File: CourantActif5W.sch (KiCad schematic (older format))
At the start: 2 parts, among them U23 ADC124S021CIMM_NOPB

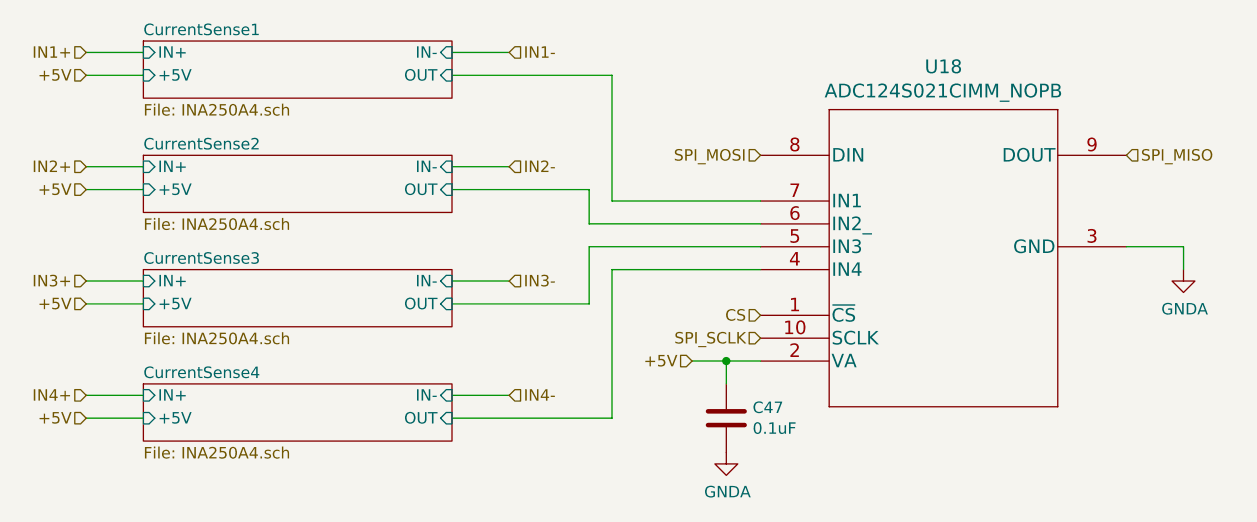
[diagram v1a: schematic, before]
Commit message: Changement pin pour switchs cannaux passifs
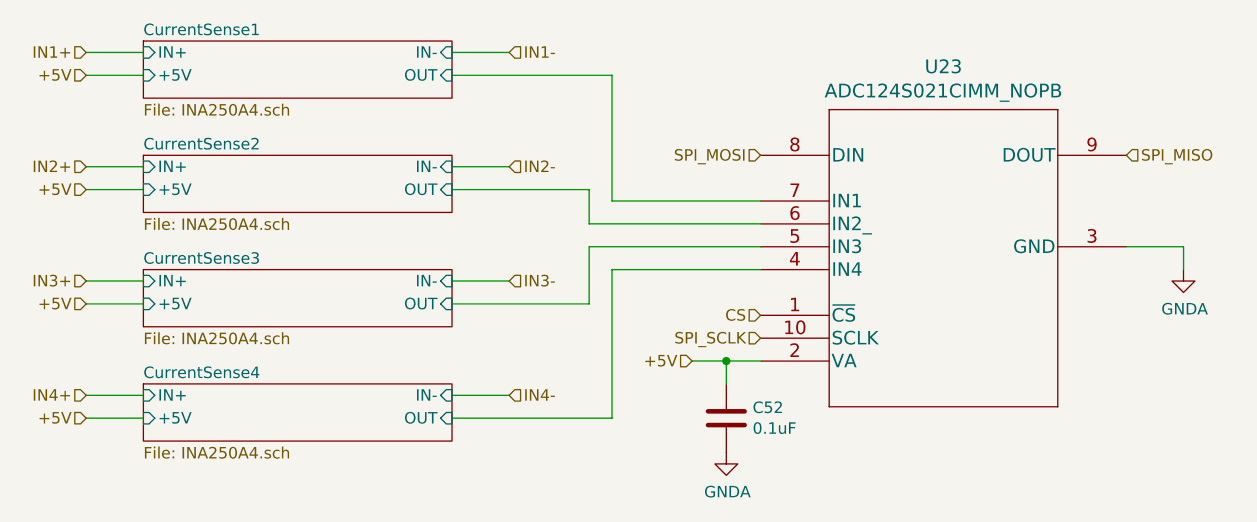
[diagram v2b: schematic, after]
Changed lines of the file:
@@
 $Descr A4 11693 8268
 encoding utf-8
-Sheet 24 80
+Sheet 29 80
 Title ""
 Date "2020-05-19"
@@
 AR Path="/5EEAF65F/5EDDD78D" Ref="U13"  Part="1"
 AR Path="/5EEC30AA/5EDDD78D" Ref="U18"  Part="1"
-F 0 "U18" H 6950 3537 60  0000 C CNN
+F 0 "U23" H 6950 3537 60  0000 C CNN
 F 1 "ADC124S021CIMM_NOPB" H 6950 3431 60  0000 C CNN
 F 2 "Package_SO:VSSOP-10_3x3mm_P0.5mm" H 6950 3390 60  0001 C CNN
@@
 AR Path="/5EEAF65F/5EDF45FB" Ref="C42"  Part="1"
 AR Path="/5EEC30AA/5EDF45FB" Ref="C47"  Part="1"
-F 0 "C47" H 6115 4346 50  0000 L CNN
+F 0 "C52" H 6115 4346 50  0000 L CNN
 F 1 "0.1uF" H 6115 4255 50  0000 L CNN
 F 2 "Capacitor_SMD:C_0402_1005Metric" H 6038 4150 50  0001 C CNN

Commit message: Routed most of the power
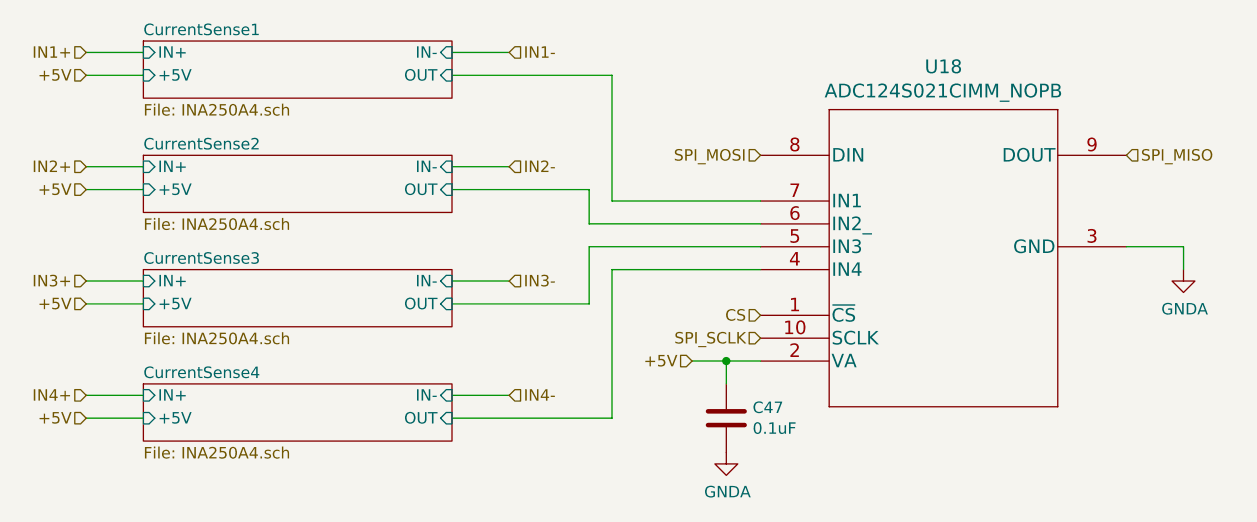
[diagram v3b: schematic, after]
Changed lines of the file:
@@
 $Descr A4 11693 8268
 encoding utf-8
-Sheet 29 80
+Sheet 24 80
 Title ""
 Date "2020-05-19"
@@
 AR Path="/5EEAF65F/5EDDD78D" Ref="U13"  Part="1"
 AR Path="/5EEC30AA/5EDDD78D" Ref="U18"  Part="1"
-F 0 "U23" H 6950 3537 60  0000 C CNN
+F 0 "U18" H 6950 3537 60  0000 C CNN
 F 1 "ADC124S021CIMM_NOPB" H 6950 3431 60  0000 C CNN
 F 2 "Package_SO:VSSOP-10_3x3mm_P0.5mm" H 6950 3390 60  0001 C CNN
@@
 AR Path="/5EEAF65F/5EDF45FB" Ref="C42"  Part="1"
 AR Path="/5EEC30AA/5EDF45FB" Ref="C47"  Part="1"
-F 0 "C52" H 6115 4346 50  0000 L CNN
+F 0 "C47" H 6115 4346 50  0000 L CNN
 F 1 "0.1uF" H 6115 4255 50  0000 L CNN
 F 2 "Capacitor_SMD:C_0402_1005Metric" H 6038 4150 50  0001 C CNN
@@
 AR Path="/5EEC30AA/618421DB" Ref="#PWR090"  Part="1"
 AR Path="/5EC4179E/618421DB" Ref="#PWR0104"  Part="1"
-F 0 "#PWR0104" H 8000 3400 50  0001 C CNN
+F 0 "#PWR090" H 8000 3400 50  0001 C CNN
 F 1 "GNDA" H 8005 3477 50  0000 C CNN
 F 2 "" H 8000 3650 50  0001 C CNN
@@
 AR Path="/5EEC30AA/61842231" Ref="#PWR089"  Part="1"
 AR Path="/5EC4179E/61842231" Ref="#PWR0103"  Part="1"
-F 0 "#PWR0103" H 6000 4200 50  0001 C CNN
+F 0 "#PWR089" H 6000 4200 50  0001 C CNN
 F 1 "GNDA" H 6005 4277 50  0000 C CNN
 F 2 "" H 6000 4450 50  0001 C CNN

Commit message: routing usb
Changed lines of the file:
@@
 $Descr A4 11693 8268
 encoding utf-8
-Sheet 24 80
+Sheet 14 80
 Title ""
 Date "2020-05-19"
@@
 AR Path="/5EEAF65F/5EDDD78D" Ref="U13"  Part="1"
 AR Path="/5EEC30AA/5EDDD78D" Ref="U18"  Part="1"
-F 0 "U18" H 6950 3537 60  0000 C CNN
+F 0 "U8" H 6950 3537 60  0000 C CNN
 F 1 "ADC124S021CIMM_NOPB" H 6950 3431 60  0000 C CNN
 F 2 "Package_SO:VSSOP-10_3x3mm_P0.5mm" H 6950 3390 60  0001 C CNN
@@
 AR Path="/5EEAF65F/5EDF45FB" Ref="C42"  Part="1"
 AR Path="/5EEC30AA/5EDF45FB" Ref="C47"  Part="1"
-F 0 "C47" H 6115 4346 50  0000 L CNN
+F 0 "C37" H 6115 4346 50  0000 L CNN
 F 1 "0.1uF" H 6115 4255 50  0000 L CNN
 F 2 "Capacitor_SMD:C_0402_1005Metric" H 6038 4150 50  0001 C CNN
@@
 AR Path="/5EEC30AA/618421DB" Ref="#PWR090"  Part="1"
 AR Path="/5EC4179E/618421DB" Ref="#PWR0104"  Part="1"
-F 0 "#PWR090" H 8000 3400 50  0001 C CNN
+F 0 "#PWR062" H 8000 3400 50  0001 C CNN
 F 1 "GNDA" H 8005 3477 50  0000 C CNN
 F 2 "" H 8000 3650 50  0001 C CNN
@@
 AR Path="/5EEC30AA/61842231" Ref="#PWR089"  Part="1"
 AR Path="/5EC4179E/61842231" Ref="#PWR0103"  Part="1"
-F 0 "#PWR089" H 6000 4200 50  0001 C CNN
+F 0 "#PWR061" H 6000 4200 50  0001 C CNN
 F 1 "GNDA" H 6005 4277 50  0000 C CNN
 F 2 "" H 6000 4450 50  0001 C CNN

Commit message: Debut routing cannaux passifs
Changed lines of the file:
@@
 $Descr A4 11693 8268
 encoding utf-8
-Sheet 14 80
+Sheet 24 80
 Title ""
 Date "2020-05-19"
@@
 AR Path="/5EEAF65F/5EDDD78D" Ref="U13"  Part="1"
 AR Path="/5EEC30AA/5EDDD78D" Ref="U18"  Part="1"
-F 0 "U8" H 6950 3537 60  0000 C CNN
+F 0 "U18" H 6950 3537 60  0000 C CNN
 F 1 "ADC124S021CIMM_NOPB" H 6950 3431 60  0000 C CNN
 F 2 "Package_SO:VSSOP-10_3x3mm_P0.5mm" H 6950 3390 60  0001 C CNN
@@
 AR Path="/5EEAF65F/5EDF45FB" Ref="C42"  Part="1"
 AR Path="/5EEC30AA/5EDF45FB" Ref="C47"  Part="1"
-F 0 "C37" H 6115 4346 50  0000 L CNN
+F 0 "C47" H 6115 4346 50  0000 L CNN
 F 1 "0.1uF" H 6115 4255 50  0000 L CNN
 F 2 "Capacitor_SMD:C_0402_1005Metric" H 6038 4150 50  0001 C CNN
@@
 AR Path="/5EEC30AA/618421DB" Ref="#PWR090"  Part="1"
 AR Path="/5EC4179E/618421DB" Ref="#PWR0104"  Part="1"
-F 0 "#PWR062" H 8000 3400 50  0001 C CNN
+F 0 "#PWR090" H 8000 3400 50  0001 C CNN
 F 1 "GNDA" H 8005 3477 50  0000 C CNN
 F 2 "" H 8000 3650 50  0001 C CNN
@@
 AR Path="/5EEC30AA/61842231" Ref="#PWR089"  Part="1"
 AR Path="/5EC4179E/61842231" Ref="#PWR0103"  Part="1"
-F 0 "#PWR061" H 6000 4200 50  0001 C CNN
+F 0 "#PWR089" H 6000 4200 50  0001 C CNN
 F 1 "GNDA" H 6005 4277 50  0000 C CNN
 F 2 "" H 6000 4450 50  0001 C CNN
